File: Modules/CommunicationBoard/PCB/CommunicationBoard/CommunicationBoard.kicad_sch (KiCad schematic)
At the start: 37 parts, among them J1 CIO_MAIN_CONNECTOR, J2 Conn_Coaxial, J3 PROGRAMMING, Q1 IRLM2502, U1 E22-900M30S, U3 ESP32-WROOM-E

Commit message: CommsBoard v1.0
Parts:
- J2: footprint Connector_Coaxial:SMA_Amphenol_132289_EdgeMount -> IcaroFootprints:SMA_132323
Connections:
- net DIO1: now also U3.5 (SENSOR_VN/GPIO39/ADC1_CH3)
- net DIO2: now also U3.4 (SENSOR_VP/GPIO36/ADC1_CH0)
- net at R2.1, U1.21 (ANT): no longer C5.1
- net at C6.1, J2.1 (In), R2.2: now also C5.1
- no-connect marks 13 -> 11
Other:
- moved on the sheet: R2
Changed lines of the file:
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@@
 	)
 	(junction
+		(at 209.55 121.92)
+		(diameter 0)
+		(color 0 0 0 0)
+	)
+	(junction
 		(at 33.02 288.29)
 		(diameter 0)
@@
 	)
 	(junction
-		(at 209.55 121.92)
-		(diameter 0)
-		(color 0 0 0 0)
-	)
-	(junction
 		(at 280.67 234.95)
 		(diameter 0)
@@
 	)
 	(no_connect
-		(at 113.03 243.84)
-	)
-	(no_connect
 		(at 179.07 251.46)
 	)
@@
 	)
 	(no_connect
-		(at 113.03 246.38)
-	)
-	(no_connect
 		(at 62.23 46.99)
 	)
@@
 	(wire
 		(pts
-			(xy 184.15 121.92) (xy 209.55 121.92)
-		)
-		(stroke
-			(width 0)
-			(type default)
-		)
-	)
-	(wire
-		(pts
 			(xy 53.34 74.93) (xy 53.34 82.55)
 		)
@@
 	(wire
 		(pts
-			(xy 53.34 59.69) (xy 62.23 59.69)
+			(xy 205.74 121.92) (xy 209.55 121.92)
 		)
 		(stroke
@@
 	(wire
 		(pts
-			(xy 242.57 38.1) (xy 233.68 38.1)
+			(xy 53.34 59.69) (xy 62.23 59.69)
 		)
 		(stroke
@@
 	(wire
 		(pts
-			(xy 217.17 121.92) (xy 219.71 121.92)
+			(xy 242.57 38.1) (xy 233.68 38.1)
 		)
 		(stroke
@@
 	(wire
 		(pts
+			(xy 106.68 243.84) (xy 113.03 243.84)
+		)
+		(stroke
+			(width 0)
+			(type default)
+		)
+	)
+	(wire
+		(pts
 			(xy 33.02 288.29) (xy 44.45 288.29)
 		)
@@
 	(wire
 		(pts
+			(xy 106.68 246.38) (xy 113.03 246.38)
+		)
+		(stroke
+			(width 0)
+			(type default)
+		)
+	)
+	(wire
+		(pts
 			(xy 87.63 74.93) (xy 97.79 74.93)
 		)
@@
 	(wire
 		(pts
-			(xy 209.55 121.92) (xy 212.09 121.92)
+			(xy 209.55 121.92) (xy 219.71 121.92)
 		)
 		(stroke
@@
 	(wire
 		(pts
+			(xy 184.15 121.92) (xy 200.66 121.92)
+		)
+		(stroke
+			(width 0)
+			(type default)
+		)
+	)
+	(wire
+		(pts
 			(xy 170.18 69.85) (xy 170.18 67.31)
 		)
@@
 		)
 	)
+	(label "DIO2"
+		(at 106.68 243.84 0)
+		(effects
+			(font
+				(size 1.27 1.27)
+			)
+			(justify left bottom)
+		)
+	)
 	(label "C_UART_RX"
 		(at 170.18 320.04 180)
@@
 		)
 	)
+	(label "DIO1"
+		(at 106.68 246.38 0)
+		(effects
+			(font
+				(size 1.27 1.27)
+			)
+			(justify left bottom)
+		)
+	)
 	(label "RXEN"
 		(at 142.24 137.16 0)
@@
 			)
 		)
-		(property "Footprint" "Connector_Coaxial:SMA_Amphenol_132289_EdgeMount"
+		(property "Footprint" "IcaroFootprints:SMA_132323"
 			(at 232.41 114.3 0)
 			(effects
@@
 	(symbol
 		(lib_id "Device:R_Small")
-		(at 214.63 121.92 90)
+		(at 203.2 121.92 90)
 		(unit 1)
 		(exclude_from_sim no)
@@
 		(fields_autoplaced yes)
 		(property "Reference" "R2"
-			(at 214.63 116.84 90)
+			(at 203.2 116.84 90)
 			(effects
 				(font
@@
 		)
 		(property "Value" "0R"
-			(at 214.63 119.38 90)
+			(at 203.2 119.38 90)
 			(effects
 				(font
@@
 		)
 		(property "Footprint" "Resistor_SMD:R_0603_1608Metric_Pad0.98x0.95mm_HandSolder"
-			(at 214.63 121.92 0)
+			(at 203.2 121.92 0)
 			(effects
 				(font
@@
 		)
 		(property "Datasheet" "~"
-			(at 214.63 121.92 0)
+			(at 203.2 121.92 0)
 			(effects
 				(font
@@
 		)
 		(property "Description" "Resistor, small symbol"
-			(at 214.63 121.92 0)
+			(at 203.2 121.92 0)
 			(effects
 				(font

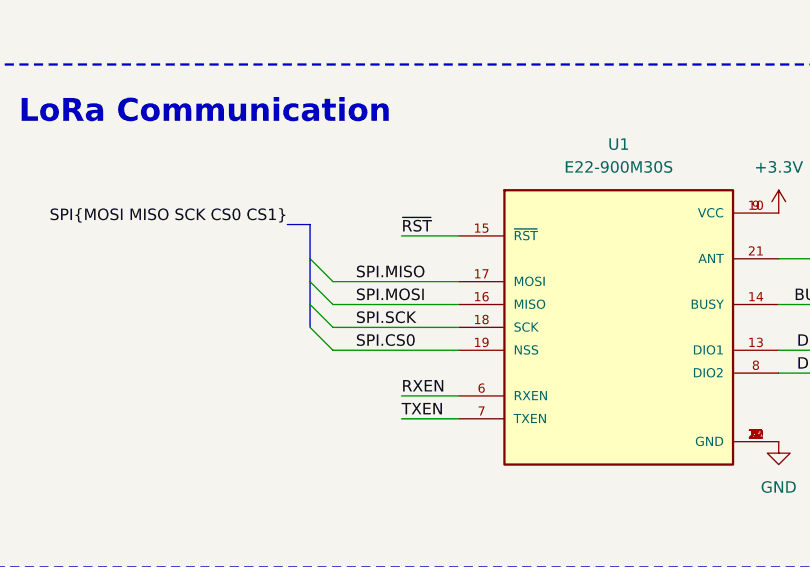
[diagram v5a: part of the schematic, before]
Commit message: Changed MISO/MOSI in Comms
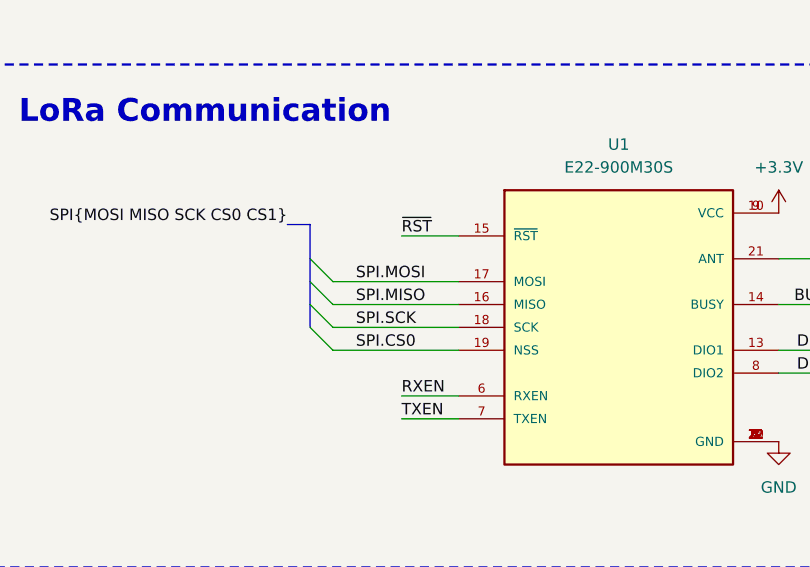
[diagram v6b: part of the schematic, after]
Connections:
- net SPI.MISO: now also U1.16 (MISO); no longer U1.17 (MOSI)
- net SPI.MOSI: now also U1.17 (MOSI); no longer U1.16 (MISO)
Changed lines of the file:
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@@
 	)
 	(label "SPI.MOSI"
-		(at 137.16 127 0)
+		(at 137.16 124.46 0)
 		(effects
 			(font
@@
 	)
 	(label "SPI.MISO"
-		(at 137.16 124.46 0)
-		(effects
-			(font
+		(at 137.16 127 0)
+		(effects
+			(font
